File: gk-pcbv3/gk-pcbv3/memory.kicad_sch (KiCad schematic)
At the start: 21 parts, among them J4 Micro_SD_Card_Det2, U6 IS42S16320F-7TLI-TR, U8 TPS2041BDBV

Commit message: v3 board
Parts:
- removed C37, C38, C39, C40: 100n, Capacitor_SMD:C_0603_1608Metric, symbol Device:C
- removed U6: IS42S16320F-7TLI-TR, Package_SO:TSOP-II-54_22.2x10.16mm_P0.8mm, symbol Memory_RAM:MT48LC16M16A2P
- added C34, C35, C60, C61, C62, C75: 100n, Capacitor_SMD:C_0603_1608Metric, symbol Device:C
- added U17, U6: S80KS5122GABHI020, STM32H7S7:PG-BGA-24-801, symbol Infineon HyperRAM:S80KS5122GABHI020
- added U5: S26KS128SDPBHM020, STM32H7S7:BGA24_S26KS512SDPBHI020_CYP_INF, symbol Infineon Flash:S26KS128SDPBHM020
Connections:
- net GND: now also C34.2, C35.2, C60.2, C61.2, C62.2, C75.2, U17.B3 (VSS), U17.C1 (VSSQ), U17.E5 (VSSQ), U5.B3 (VSS), U5.C1 (VSSQ), U5.E5 (VSSQ), U6.B3 (VSS), U6.C1 (VSSQ), U6.E5 (VSSQ)
- net VCC: no longer C41.1, C42.1, C43.1
- new net +1V8: C34.1, C35.1, C41.1, C42.1, C43.1, C60.1, C61.1, C62.1, C75.1, U17.B4 (VCC), U17.D1 (VCCQ), U17.E4 (VCCQ), U5.B4 (VCC), U5.D1 (VCCQ), U5.E4 (VCCQ), U6.B4 (VCC), U6.D1 (VCCQ), U6.E4 (VCCQ)
- new net XPSI2_RESET#: U5.A4 (RESET#)
- new net XSPI1_CK: U17.B2 (CK), U6.B2 (CK)
- new net XSPI1_CK#: U17.B1 (CK#), U6.B1 (CK#)
- new net XSPI1_CS#: U17.A3 (CS#), U6.A3 (CS#)
- new net XSPI1_DQ0: U6.D3 (DQ0)
- new net XSPI1_DQ1: U6.D2 (DQ1)
- new net XSPI1_DQ10: U17.C4 (DQ2)
- new net XSPI1_DQ11: U17.D4 (DQ3)
- new net XSPI1_DQ12: U17.D5 (DQ4)
- new net XSPI1_DQ13: U17.E3 (DQ5)
- new net XSPI1_DQ14: U17.E2 (DQ6)
- new net XSPI1_DQ15: U17.E1 (DQ7)
- new net XSPI1_DQ2: U6.C4 (DQ2)
- new net XSPI1_DQ3: U6.D4 (DQ3)
- new net XSPI1_DQ4: U6.D5 (DQ4)
- new net XSPI1_DQ5: U6.E3 (DQ5)
- new net XSPI1_DQ6: U6.E2 (DQ6)
- new net XSPI1_DQ7: U6.E1 (DQ7)
- new net XSPI1_DQ8: U17.D3 (DQ0)
- new net XSPI1_DQ9: U17.D2 (DQ1)
- new net XSPI1_RESET#: U17.A4 (RESET#), U6.A4 (RESET#)
- new net XSPI1_RWDS0: U6.C3 (RWDS)
- new net XSPI1_RWDS1: U17.C3 (RWDS)
- new net XSPI2_CK: U5.B2 (CK)
- new net XSPI2_CK#: U5.B1 (CK#)
- new net XSPI2_CS#: U5.C2 (CS#)
- new net XSPI2_DQ0: U5.D3 (DQ0)
- new net XSPI2_DQ1: U5.D2 (DQ1)
- new net XSPI2_DQ2: U5.C4 (DQ2)
- new net XSPI2_DQ3: U5.D4 (DQ3)
- new net XSPI2_DQ4: U5.D5 (DQ4)
- new net XSPI2_DQ5: U5.E3 (DQ5)
- new net XSPI2_DQ6: U5.E2 (DQ6)
- new net XSPI2_DQ7: U5.E1 (DQ7)
- new net XSPI2_RWDS: U5.C3 (RWDS)
- no-connect marks 2 -> 6
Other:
- note added: "Flash"
- note added: "SDRAM Dual octo-SPI configuration"
- note removed: "SDRAM"

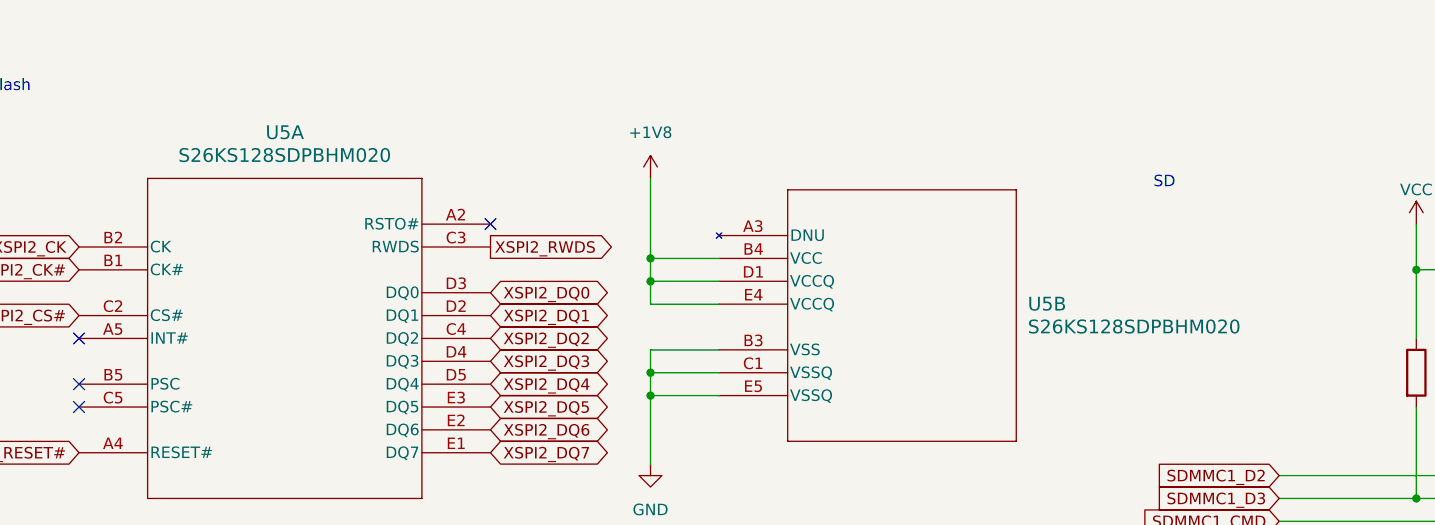
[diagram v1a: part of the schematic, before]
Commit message: schematic update
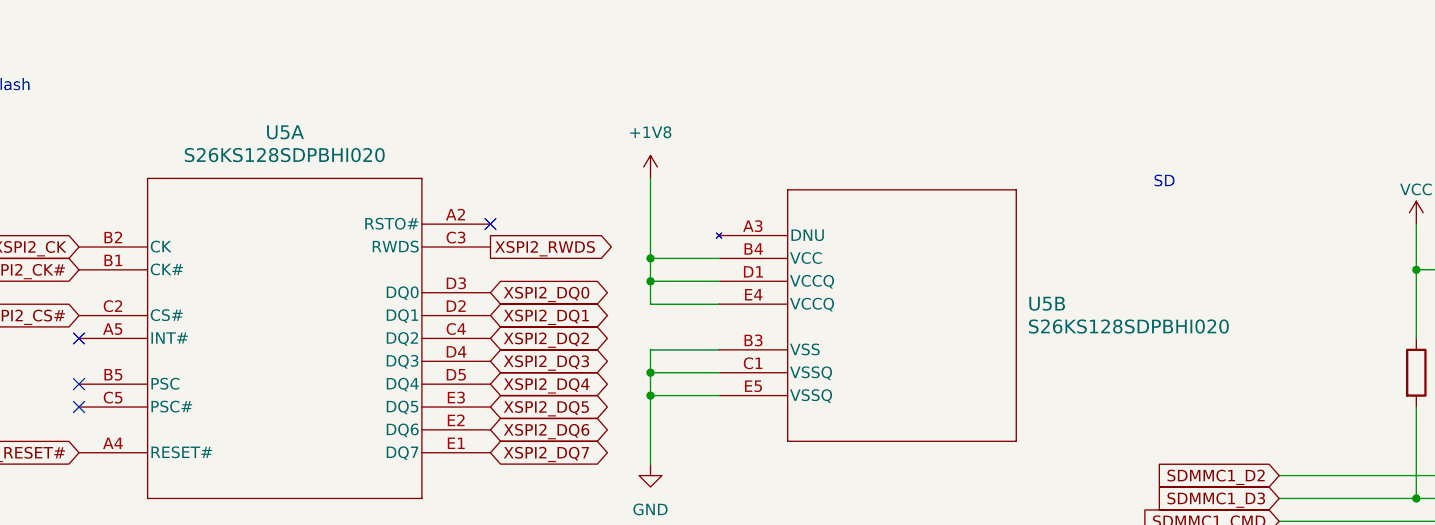
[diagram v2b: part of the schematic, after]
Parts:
- U5: value S26KS128SDPBHM020 -> S26KS128SDPBHI020
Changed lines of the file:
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@@
 			)
 		)
-		(property "Value" "S26KS128SDPBHM020"
+		(property "Value" "S26KS128SDPBHI020"
 			(at 137.16 46.9899 0)
 			(effects
@@
 			)
 		)
-		(property "Value" "S26KS128SDPBHM020"
+		(property "Value" "S26KS128SDPBHI020"
 			(at 54.61 27.94 0)
 			(effects
